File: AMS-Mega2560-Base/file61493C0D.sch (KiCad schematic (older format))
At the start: 28 parts, among them IC1 LM2670SX-5.0_NOPB, IC18 TL071CP, IC2 LM2597MX-ADJ_NOPB, J1 Screw_Terminal_01x02, Q1 IRF9Z34NPBF, U1 BK_HTC-15M

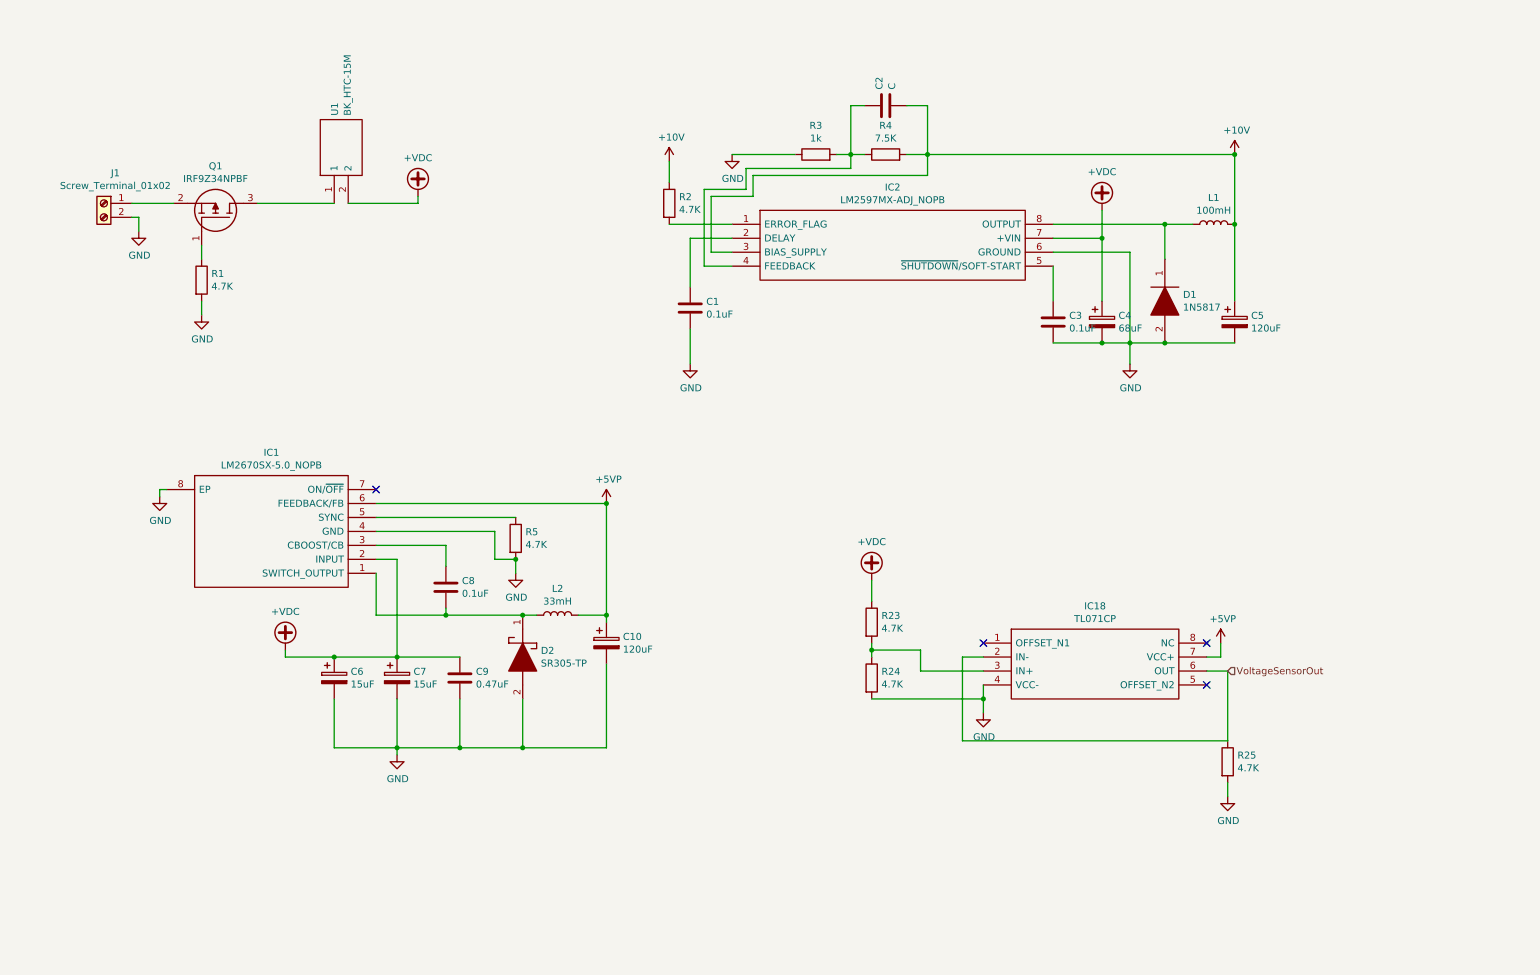
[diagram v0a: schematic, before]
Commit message: fixed the schematics for the RTC, IO and COMs. Realigned the RTD to screw term. need to finish the 3.3v portion of the power systems.
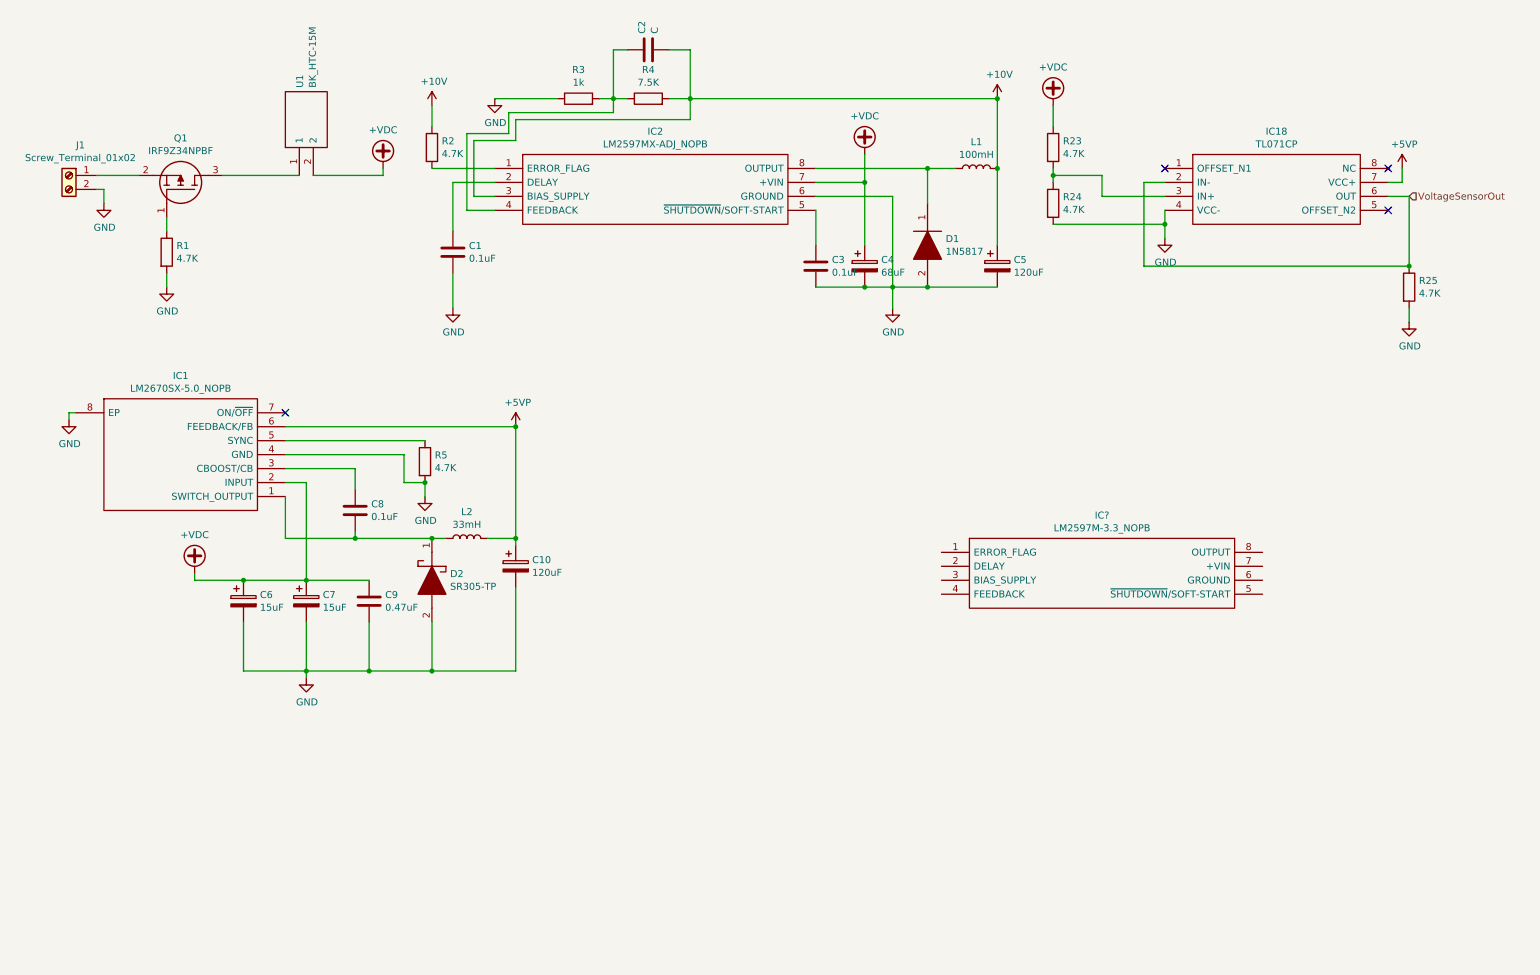
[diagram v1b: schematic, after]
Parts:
- added IC?: LM2597M-3.3_NOPB, SOIC127P600X175-8N, symbol SamacSys_Parts:LM2597M-3.3_NOPB
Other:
- moved on the sheet: C1, C10, C2, C3, C4, C5, C6, C7, C8, C9, D1, D2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

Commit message: wip working on it.
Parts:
- added C40, C41: 0.1uF, Capacitor_THT:C_Rect_L9.0mm_W3.6mm_P7.50mm_MKT, symbol Device:C
- added C42: 68uF, Capacitor_THT:CP_Radial_D5.0mm_P2.50mm, symbol Device:CP
- added C43: 120uF, Capacitor_THT:CP_Radial_D8.0mm_P5.00mm, symbol Device:CP
- added D4: 1N5817, SamacSys_Parts:DIOAD1414W86L464D238, symbol SamacSys_Parts:1N5817
- added J28: Conn_01x05, symbol Connector_Generic:Conn_01x05
- added L4: 100mH, Inductor_THT:L_Axial_L9.5mm_D4.0mm_P15.24mm_Horizontal_Fastron_SMCC, symbol Device:L
- added R42: 4.7K, Resistor_THT:R_Axial_DIN0207_L6.3mm_D2.5mm_P2.54mm_Vertical, symbol Device:R
- gave numbers to parts that had none: 1
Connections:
- net +5VP: now also J28.4 (Pin_4)
- net +VDC: now also IC21.7 (+VIN), C42.1, J28.3 (Pin_3)
- net GND: now also IC21.6 (GROUND), C40.2, C41.2, C42.2, C43.2, D4.2, J28.1 (Pin_1), J28.2 (Pin_2)
- net at IC21.1 (ERROR_FLAG): now also R42.2
- net at IC21.2 (DELAY): now also C40.1
- net at IC21.5 (~SHUTDOWN~/SOFT-START): now also C41.1
- net at IC21.8 (OUTPUT): now also D4.1, L4.1
- new net +3.3VP: C43.1, J28.5 (Pin_5), L4.2, R42.1
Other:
- moved on the sheet: IC21

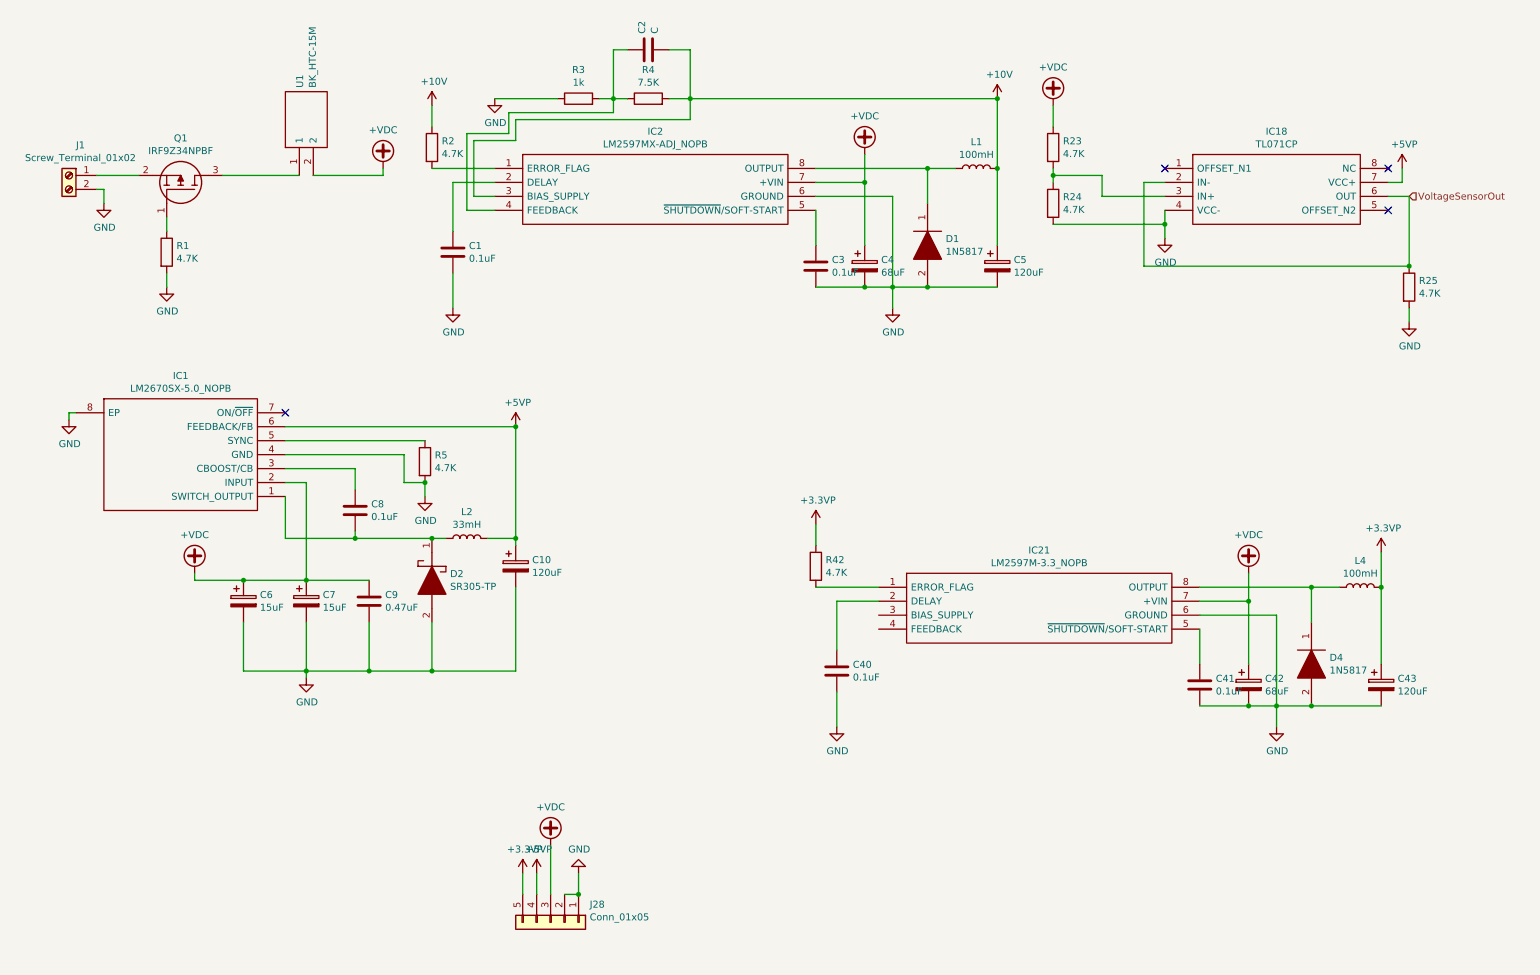
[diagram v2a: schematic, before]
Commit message: rearranging some of the hw design before i rename the repo.
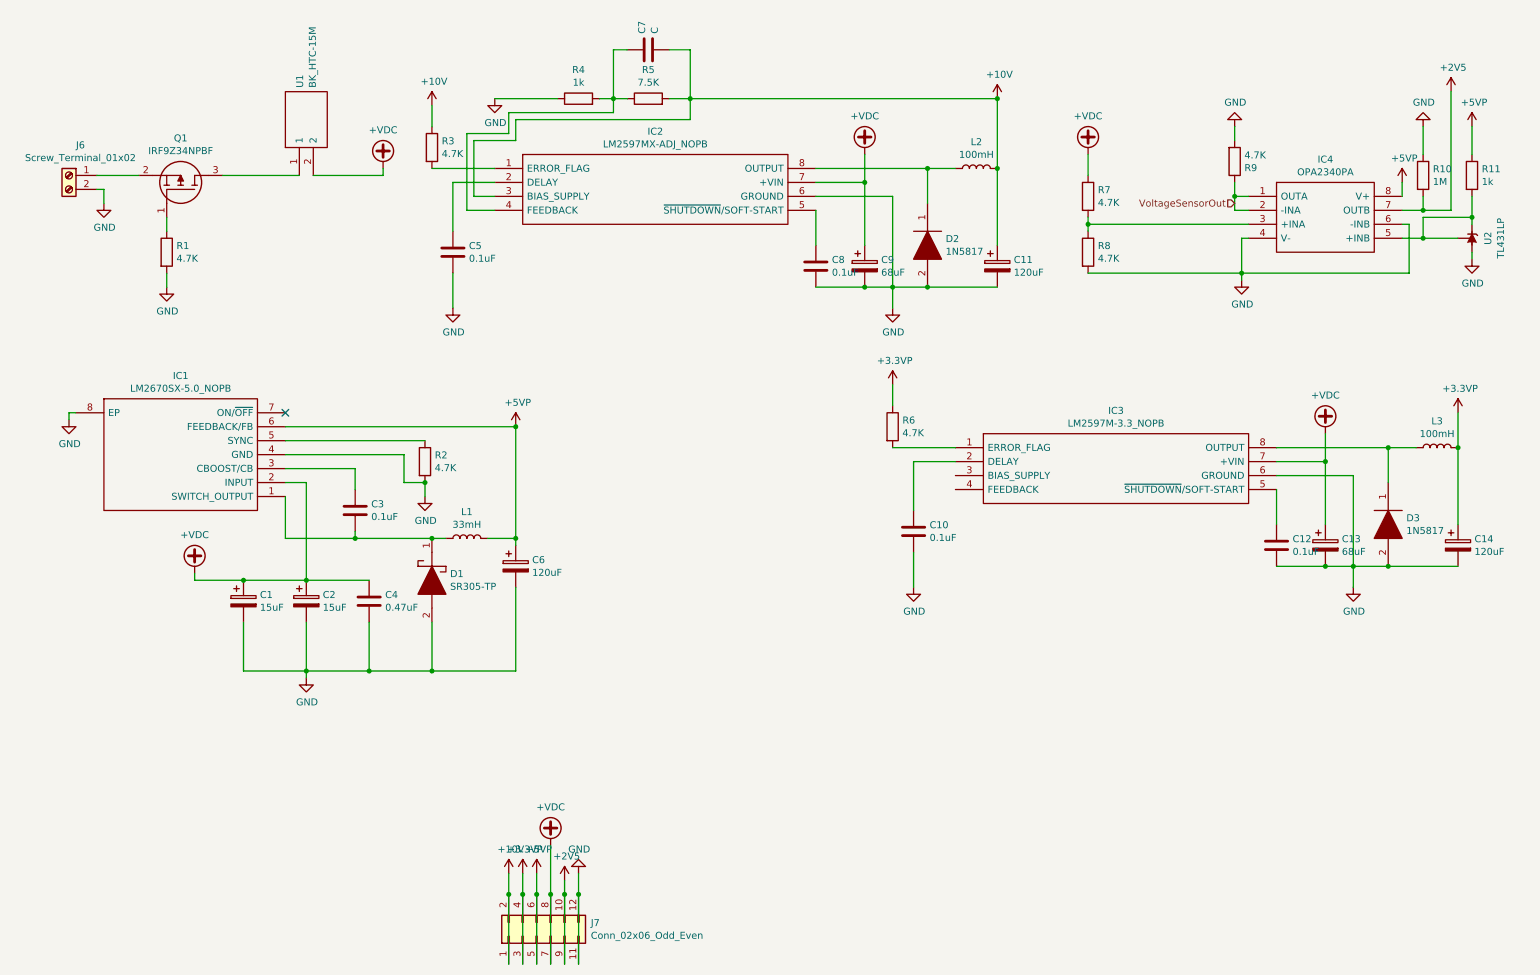
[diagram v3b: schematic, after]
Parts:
- removed IC18: TL071CP, SamacSys_Parts:DIP794W53P254L959H508Q8N, symbol SamacSys_Parts:TL071CP
- removed J28: Conn_01x05, symbol Connector_Generic:Conn_01x05
- added IC4: OPA2340PA, SamacSys_Parts:DIP794W53P254L959H508Q8N, symbol SamacSys_Parts:OPA2340PA
- added J7: Conn_02x06_Odd_Even, Connector_PinSocket_2.54mm:PinSocket_2x06_P2.54mm_Vertical, symbol Connector_Generic:Conn_02x06_Odd_Even
- added R10: 1M, Resistor_THT:R_Axial_DIN0207_L6.3mm_D2.5mm_P5.08mm_Vertical, symbol Device:R
- added R11: 1k, Resistor_THT:R_Axial_DIN0207_L6.3mm_D2.5mm_P5.08mm_Vertical, symbol Device:R
- added U2: TL431LP, Package_TO_SOT_THT:TO-92_Inline, symbol Reference_Voltage:TL431LP
- IC3: renamed from IC21; footprint SOIC127P600X175-8N -> SamacSys_Parts:SOIC127P600X175-8N
- renumbered C6 to C1, C40 to C10, C5 to C11, C41 to C12, C42 to C13, C43 to C14, C7 to C2, C8 to C3, C9 to C4, C1 to C5, C10 to C6, C2 to C7, C3 to C8, C4 to C9, D2 to D1, D1 to D2, D4 to D3, J1 to J6, L2 to L1, L1 to L2, L4 to L3, R5 to R2, R2 to R3, R3 to R4, R4 to R5, R42 to R6, R23 to R7, R24 to R8, R25 to R9
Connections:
- net +10V: now also J7.1 (Pin_1), J7.2 (Pin_2)
- net +3.3VP: now also J7.3 (Pin_3), J7.4 (Pin_4)
- net +5VP: now also IC4.8 (V+), J7.5 (Pin_5), J7.6 (Pin_6), R11.1
- net +VDC: now also J7.7 (Pin_7), J7.8 (Pin_8)
- net GND: now also IC4.4 (V-), IC4.6 (-INB), J7.11 (Pin_11), J7.12 (Pin_12), R10.1, U2.2 (A)
- net VoltageSensorOut: now also IC4.1 (OUTA), IC4.2 (-INA)
- net at R7.2, R8.1: now also IC4.3 (+INA)
- new net: IC4.5 (+INB), R11.2, U2.1 (REF), U2.3 (K)
- new net +2V5: IC4.7 (OUTB), J7.10 (Pin_10), J7.9 (Pin_9), R10.2
- no-connect marks 4 -> 1
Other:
- moved on the sheet: C10, C12, C13, C14, D3, IC3, L3, R6, R7, R8, R9
